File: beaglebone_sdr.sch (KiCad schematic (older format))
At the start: 0 parts

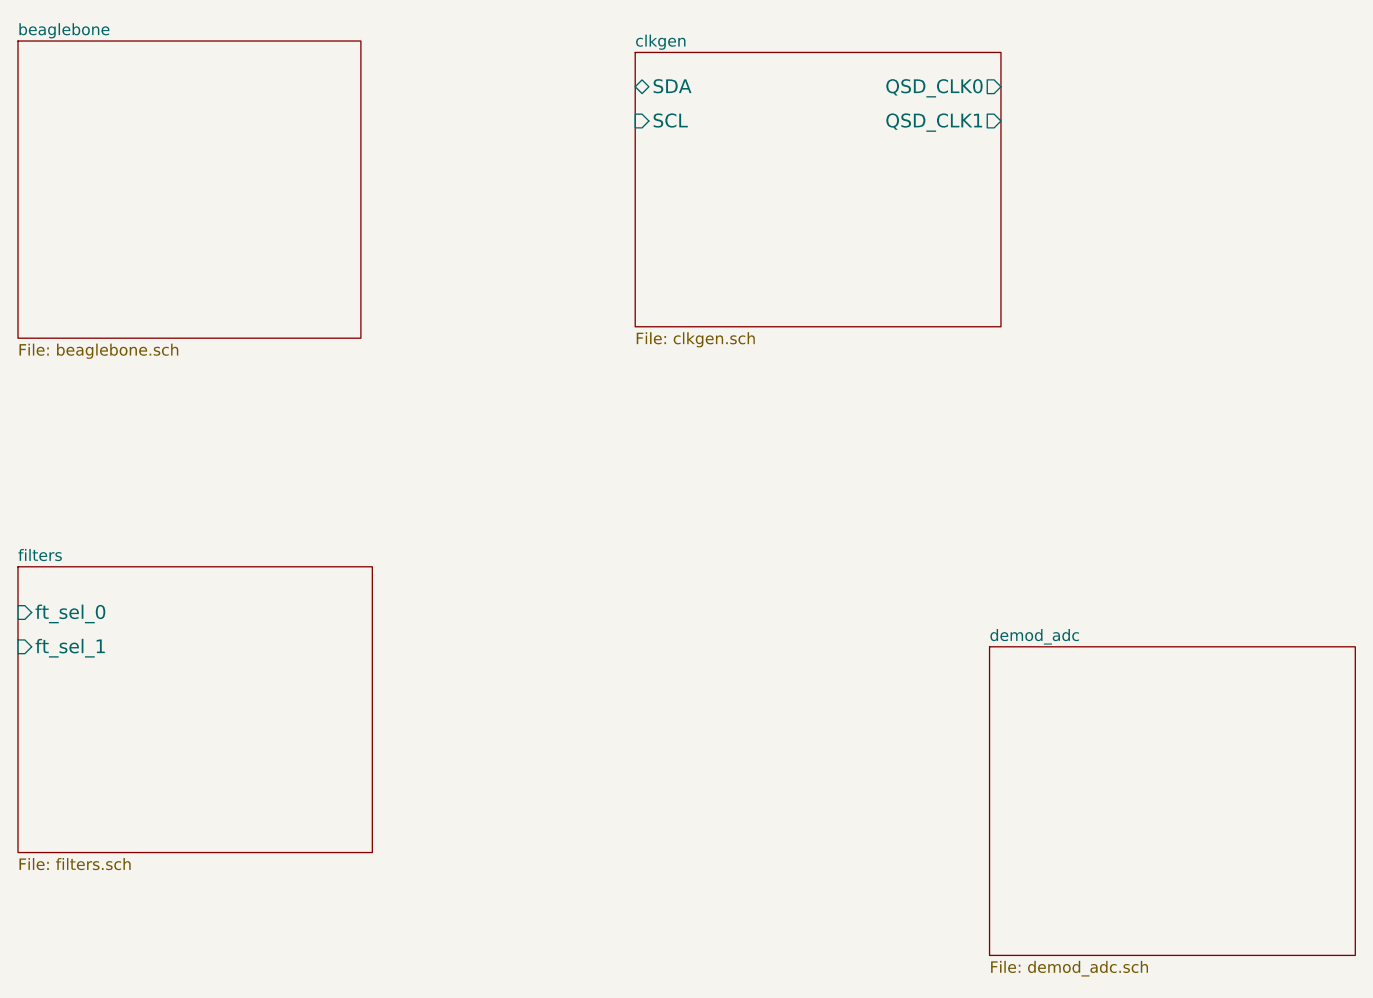
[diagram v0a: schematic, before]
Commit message: Finished filters page, started demod
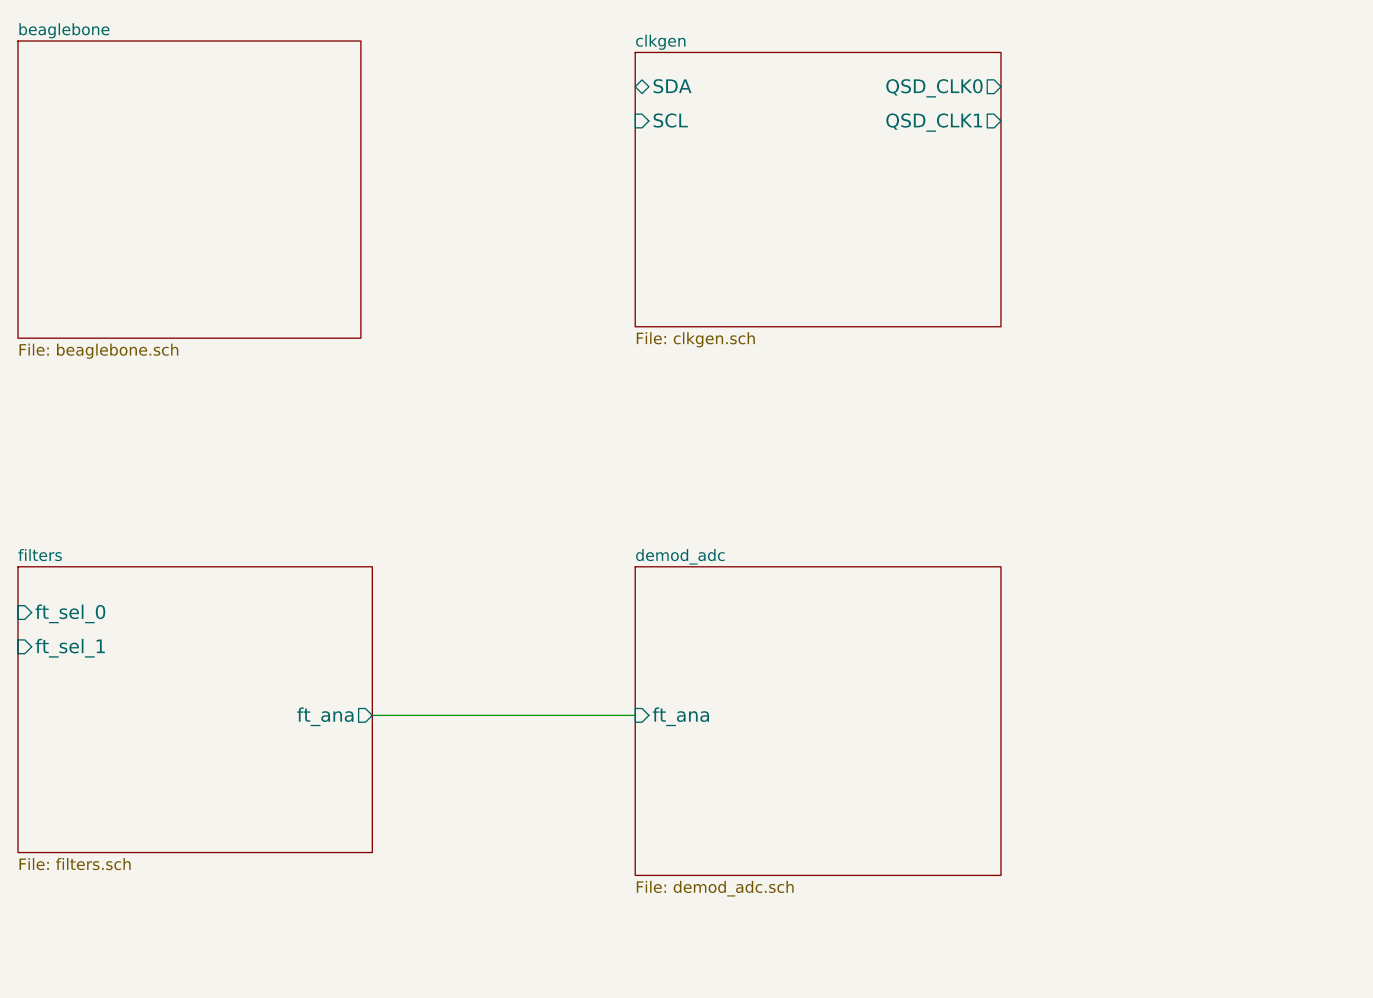
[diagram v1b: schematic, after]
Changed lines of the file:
@@
 LIBS:cmos4000
 LIBS:adc-dac
-LIBS:memory
 LIBS:special
 LIBS:analog_switches
@@
 LIBS:tsop
 LIBS:varistor
-LIBS:vishay
-LIBS:vishay_tsal4400_bpw85c
-LIBS:vishay-1
 LIBS:v-reg
-LIBS:v-reg-2
-LIBS:v-reg-fairchild
-LIBS:v-reg-lowdrop
 LIBS:si570
 LIBS:blackrock_components
@@
 Sheet 1 5
 Title ""
-Date "16 oct 2014"
+Date "19 oct 2014"
 Rev ""
 Comp ""
@@
 F2 "ft_sel_0" I L 1800 3650 60
 F3 "ft_sel_1" I L 1800 3800 60
+F4 "ft_ana" O R 3350 4100 60
 $EndSheet
 $Sheet
-S 6050 3800 1600 1350
+S 4500 3450 1600 1350
 U 53D568FE
 F0 "demod_adc" 50
 F1 "demod_adc.sch" 50
+F2 "ft_ana" I L 4500 4100 60
 $EndSheet
+Wire Wire Line
+	3350 4100 4500 4100
 $EndSCHEMATC
